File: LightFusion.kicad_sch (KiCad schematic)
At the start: 6 parts, among them U1 BMD-350-A-R

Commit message: error check passed
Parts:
- J_PROG1: footprint LightFusion:TC2030IDCFP -> LightFusion:TC2030IDCNL; symbol TC2030-IDC-NL:TC2030-IDC-FP -> TC2030-IDC-NL:TC2030-IDC-NL; Manufacturer_Part_Number TC2030-IDC-FP -> TC2030-IDC-NL
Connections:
- net GND: no longer J_PROG1.6
- net ADC_MISO: now reaches U1.10 (P0.17)
- net ADC_SCK: now reaches U1.11 (P0.15)
- net ADC_CS_N: now reaches U1.13 (P0.12)
- net ADC_DRDY_N: now reaches U1.42 (P0.19)
- net ADC_MOSI: now reaches U1.8 (P0.18)
- no-connect marks 26 -> 22
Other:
- added sheet PD_ADC (PD_ADC.kicad_sch)
- moved on the sheet: C_M1, C_M2, J_PROG1, R1, R2, U1

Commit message: placement finished on PCB
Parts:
- C_M1, C_M2: footprint LightFusion:C_0402_1005Metric -> LightFusion:C_0603_1608Metric
- R1, R2: footprint LightFusion:R_0402_1005Metric -> LightFusion:R_0603_1608Metric
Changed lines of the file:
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@@
 			)
 		)
-		(property "Footprint" "LightFusion:R_0402_1005Metric"
+		(property "Footprint" "LightFusion:R_0603_1608Metric"
 			(at 58.42 78.74 0)
 			(hide yes)
@@
 			)
 		)
-		(property "Footprint" "LightFusion:C_0402_1005Metric"
+		(property "Footprint" "LightFusion:C_0603_1608Metric"
 			(at 147.32 63.5 0)
 			(hide yes)
@@
 			)
 		)
-		(property "Footprint" "LightFusion:C_0402_1005Metric"
+		(property "Footprint" "LightFusion:C_0603_1608Metric"
 			(at 138.43 63.5 0)
 			(hide yes)
@@
 			)
 		)
-		(property "Footprint" "LightFusion:R_0402_1005Metric"
+		(property "Footprint" "LightFusion:R_0603_1608Metric"
 			(at 52.07 83.82 0)
 			(hide yes)

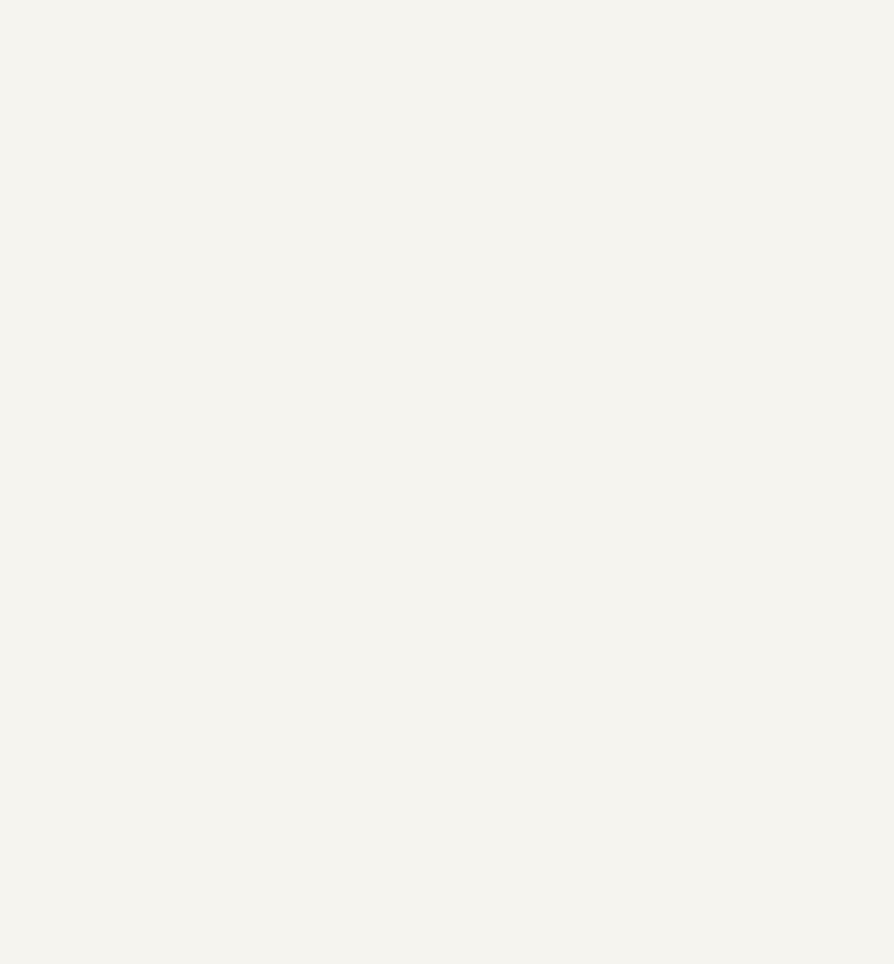
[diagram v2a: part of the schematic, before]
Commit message: eeg ic was added
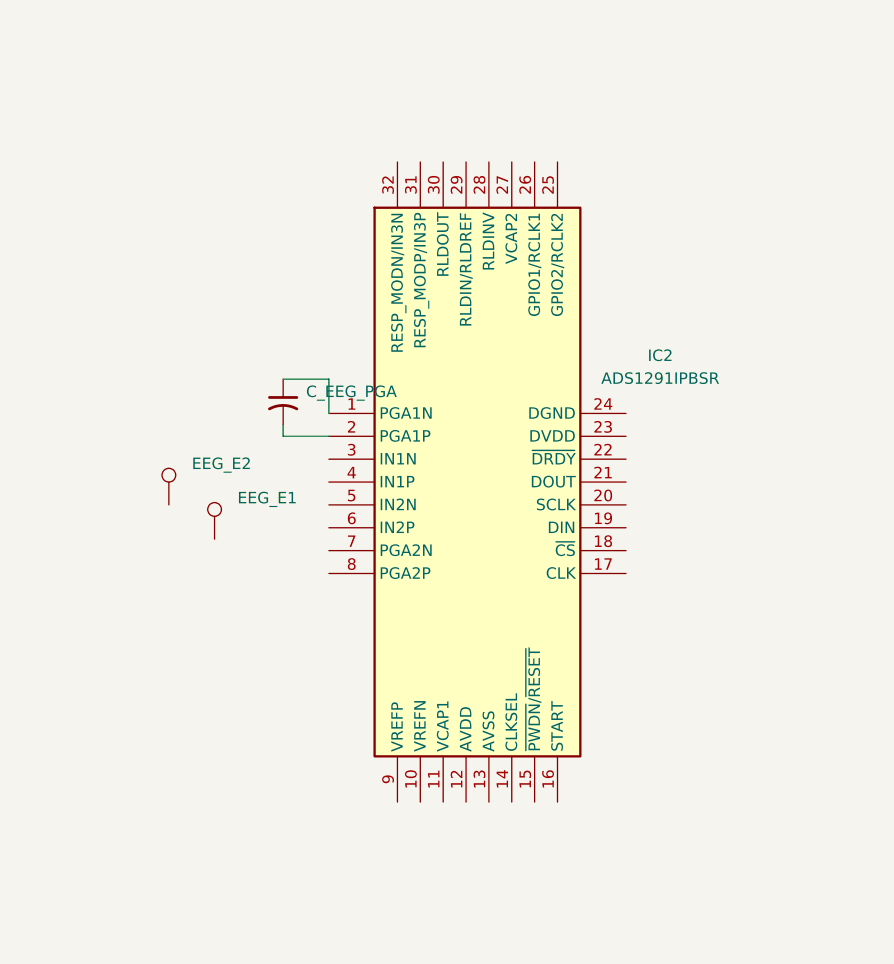
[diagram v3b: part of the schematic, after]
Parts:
- added C_EEG_PGA: 4.7 nF, LightFusion:C_0402_1005Metric, symbol C_Small_US:C_Small_US
- added EEG_E1, EEG_E2: TestPoint, symbol TestPoint:TestPoint
- added IC2: ADS1291IPBSR, LightFusion:ADS1291IPBSR, symbol ADS1291IPBSR:ADS1291IPBSR
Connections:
- new net: C_EEG_PGA.1, IC2.1 (PGA1N)
- new net: C_EEG_PGA.2, IC2.2 (PGA1P)

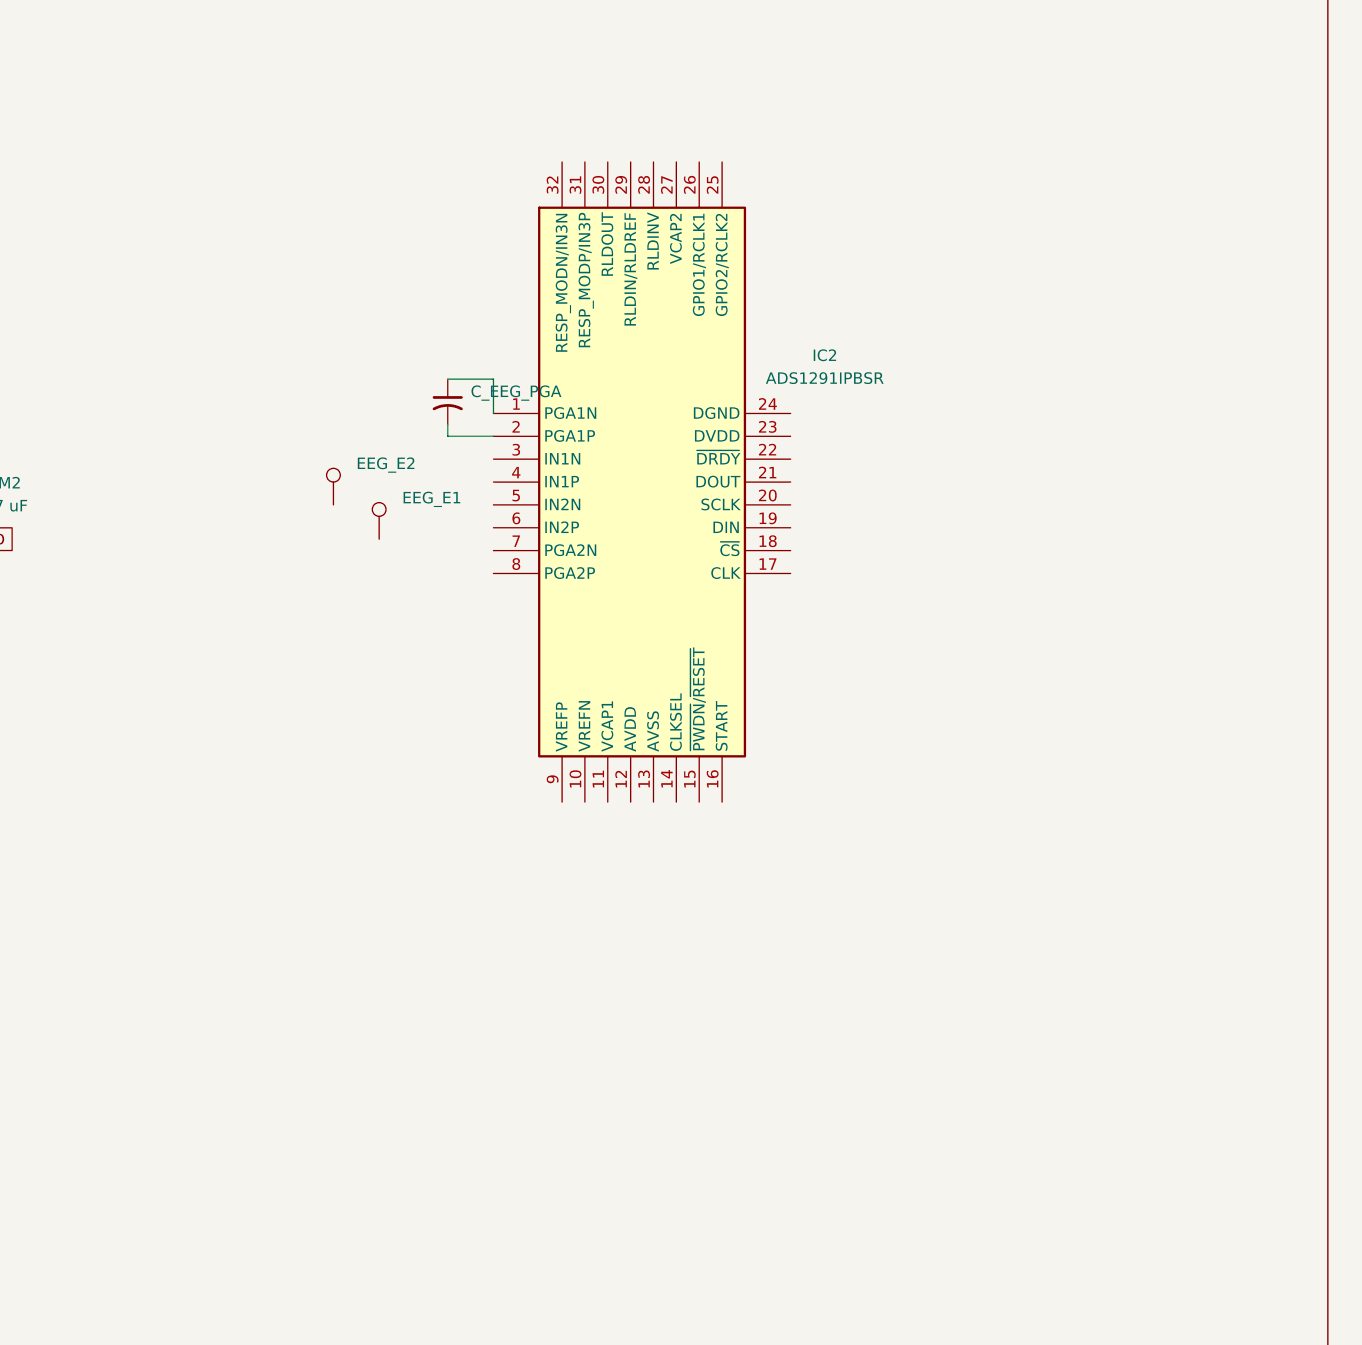
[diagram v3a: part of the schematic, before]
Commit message: added res, cap, ferrite to eeg part
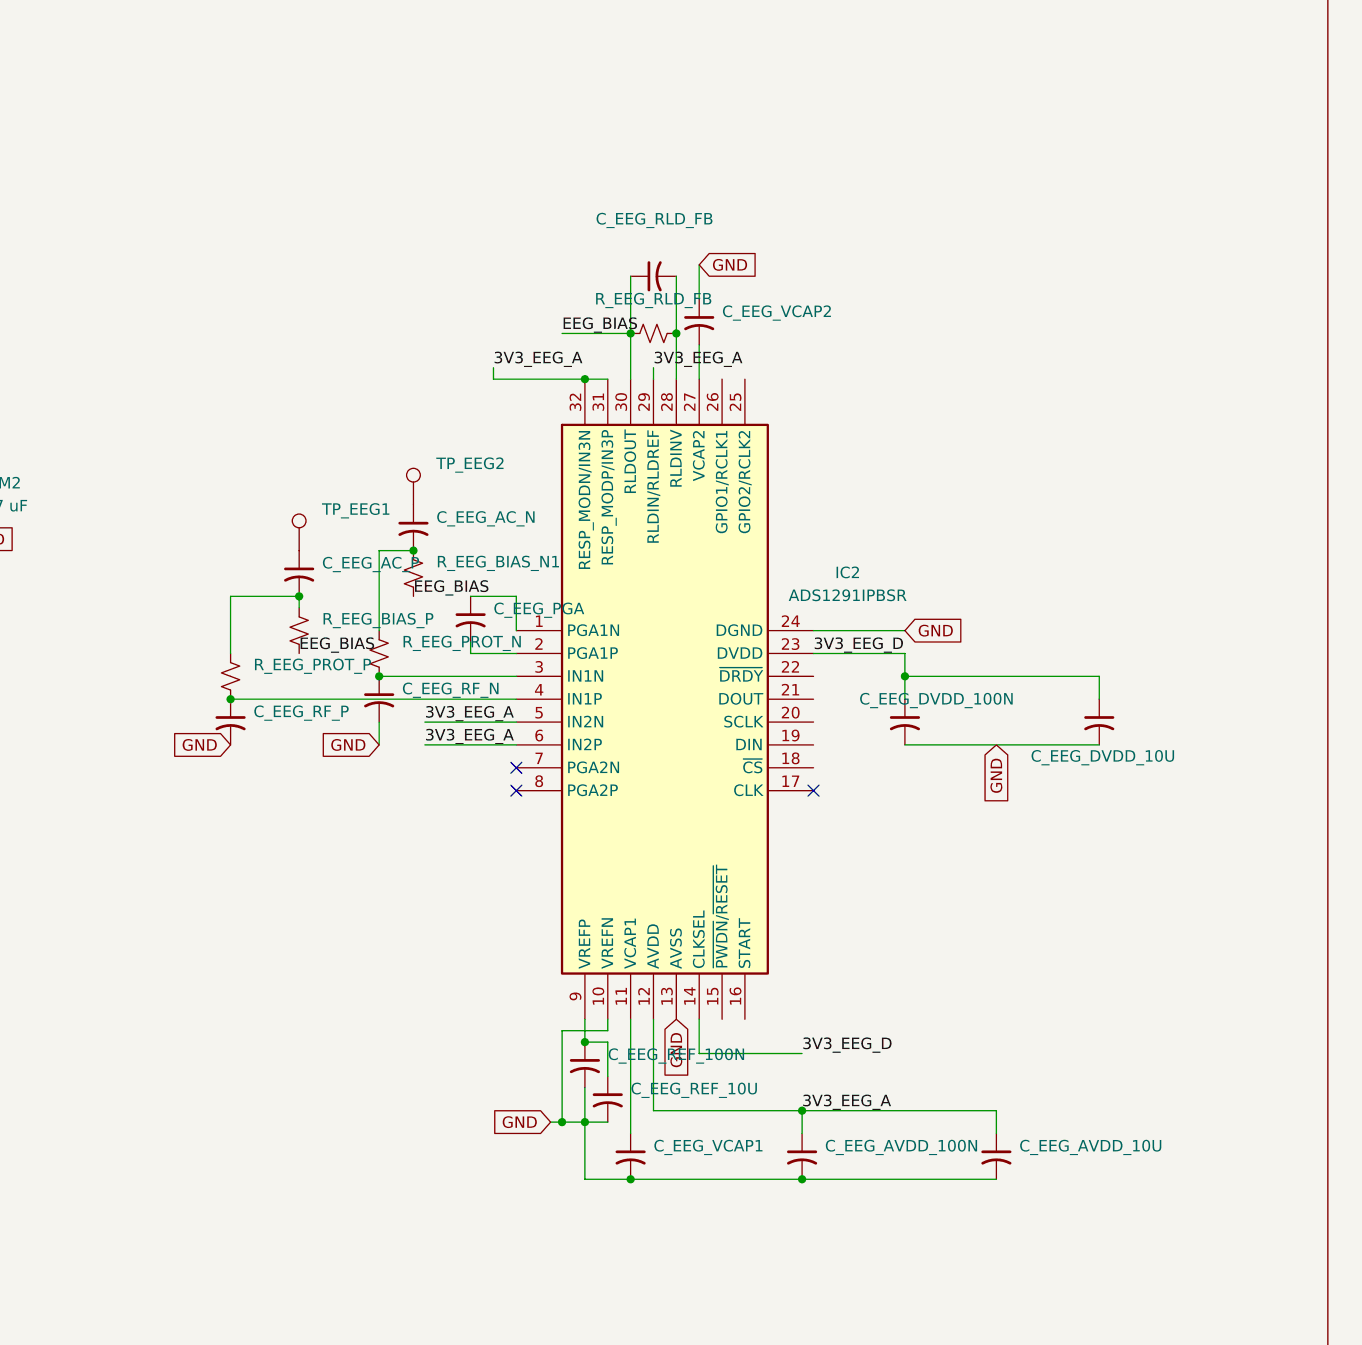
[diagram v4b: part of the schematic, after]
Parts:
- added C_EEG_AC_N, C_EEG_AC_P: 47 nF, symbol C_Small_US:C_Small_US
- added C_EEG_AVDD_100N, C_EEG_DVDD_100N, C_EEG_REF_100N: 100 nF, symbol C_Small_US:C_Small_US
- added C_EEG_AVDD_10U, C_EEG_DVDD_10U, C_EEG_REF_10U: 10 µF, symbol C_Small_US:C_Small_US
- added C_EEG_RF_N, C_EEG_RF_P: 47 pF, symbol C_Small_US:C_Small_US
- added C_EEG_RLD_FB: 1.5 nF, symbol C_Small_US:C_Small_US
- added C_EEG_VCAP1, C_EEG_VCAP2: 1 µF, symbol C_Small_US:C_Small_US
- added R_EEG_BIAS_N1, R_EEG_BIAS_P: 22 MΩ, symbol R_Small_US:R_Small_US
- added R_EEG_PROT_N, R_EEG_PROT_P: 51 kΩ, symbol R_Small_US:R_Small_US
- added R_EEG_RLD_FB: 1 MΩ, symbol R_Small_US:R_Small_US
- renumbered EEG_E1 to TP_EEG1, EEG_E2 to TP_EEG2
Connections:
- net GND: now also IC2.10 (VREFN), IC2.13 (AVSS), IC2.24 (DGND), C_EEG_AVDD_100N.2, C_EEG_AVDD_10U.2, C_EEG_DVDD_100N.2, C_EEG_DVDD_10U.2, C_EEG_REF_100N.2, C_EEG_REF_10U.2, C_EEG_RF_N.2, C_EEG_RF_P.2, C_EEG_VCAP1.2, C_EEG_VCAP2.1
- net at TP_EEG1.1: now also C_EEG_AC_P.1
- net at TP_EEG2.1: now also C_EEG_AC_N.1
- net at IC2.11 (VCAP1): now also C_EEG_VCAP1.1
- net 3V3_EEG_A: now reaches IC2.12 (AVDD)
- net 3V3_EEG_A: now also IC2.29 (RLDIN/RLDREF), IC2.31 (RESP_MODP/IN3P), IC2.32 (RESP_MODN/IN3N), IC2.5 (IN2N), IC2.6 (IN2P), C_EEG_AVDD_100N.1, C_EEG_AVDD_10U.1
- net 3V3_EEG_D: now reaches IC2.14 (CLKSEL)
- net 3V3_EEG_D: now also IC2.23 (DVDD), C_EEG_DVDD_100N.1, C_EEG_DVDD_10U.1
- net at IC2.27 (VCAP2): now also C_EEG_VCAP2.2
- net at IC2.28 (RLDINV): now also C_EEG_RLD_FB.2, R_EEG_RLD_FB.2
- net at IC2.3 (IN1N): now also C_EEG_RF_N.1, R_EEG_PROT_N.2
- net EEG_BIAS: now reaches IC2.30 (RLDOUT)
- net EEG_BIAS: now also C_EEG_RLD_FB.1, R_EEG_BIAS_N1.2, R_EEG_BIAS_P.2, R_EEG_RLD_FB.1
- net at IC2.4 (IN1P): now also C_EEG_RF_P.1, R_EEG_PROT_P.2
- net at IC2.9 (VREFP): now also C_EEG_REF_100N.1, C_EEG_REF_10U.1
- new net: C_EEG_AC_N.2, R_EEG_BIAS_N1.1, R_EEG_PROT_N.1
- new net: C_EEG_AC_P.2, R_EEG_BIAS_P.1, R_EEG_PROT_P.1
- no-connect marks 22 -> 25
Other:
- moved on the sheet: C_EEG_PGA, IC2, TP_EEG1, TP_EEG2
